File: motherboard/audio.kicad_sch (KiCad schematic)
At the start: 29 parts, among them CN1 PJ-332A-6A (3.5mm Jack), J3 RIGHT SPEAKERS, J4 LEFT SPEAKERS, Q12 2SK3018W, U23 TPA2028D1YZFT, U25 TPA2028D1YZFT

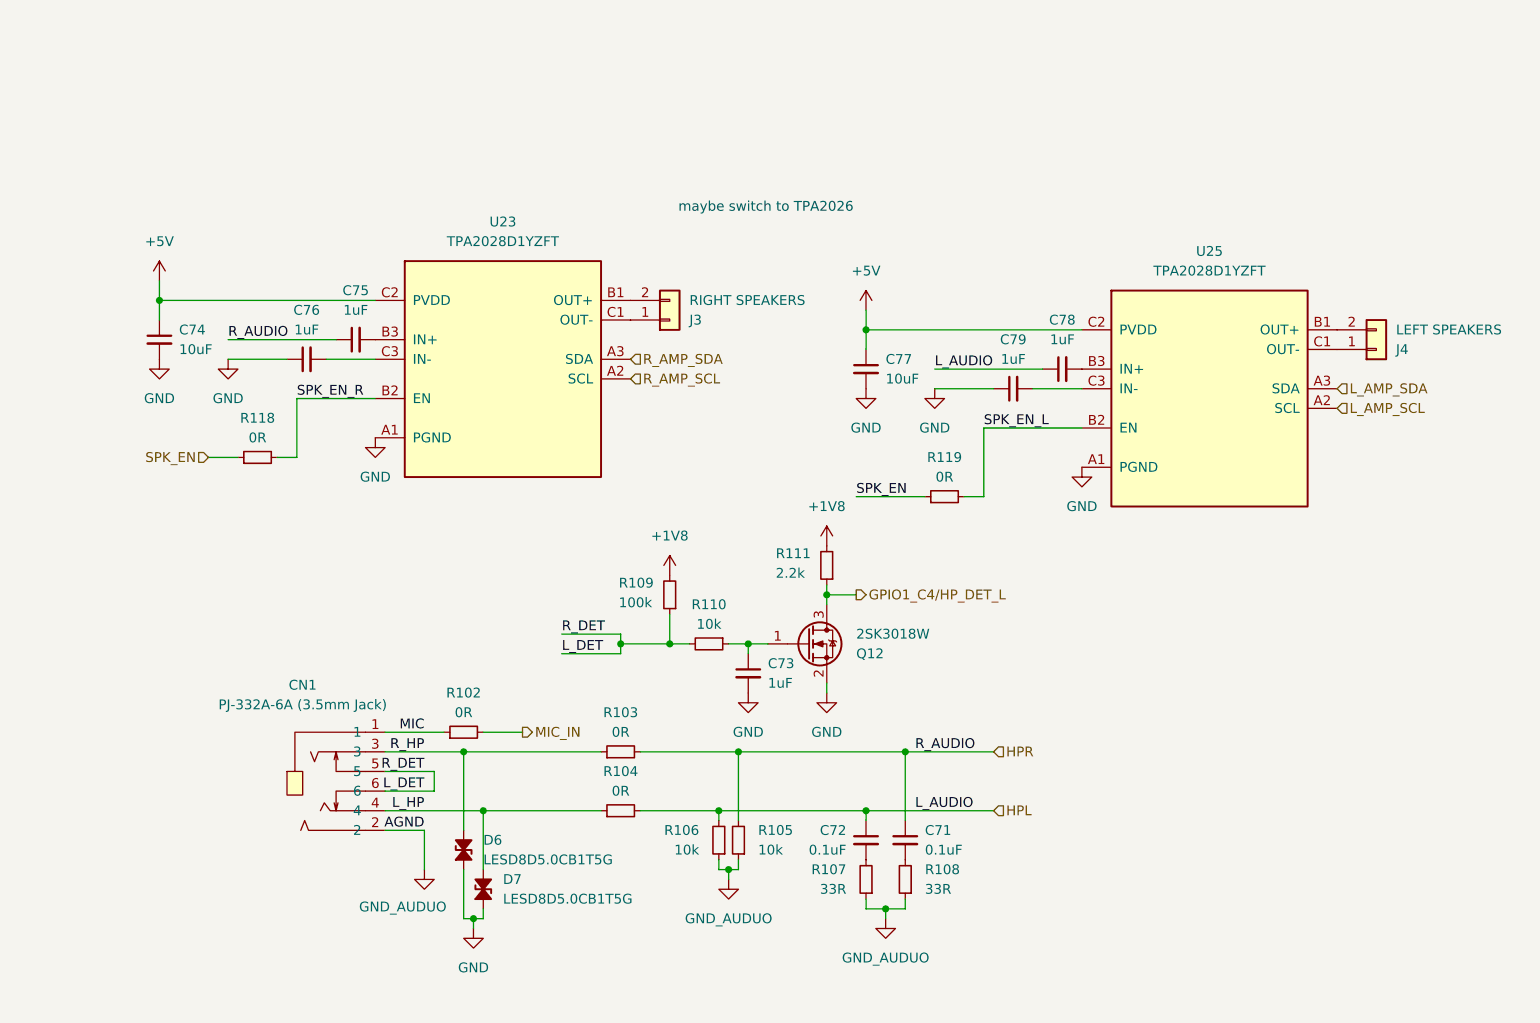
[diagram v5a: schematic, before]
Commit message: added two more display eval test boards
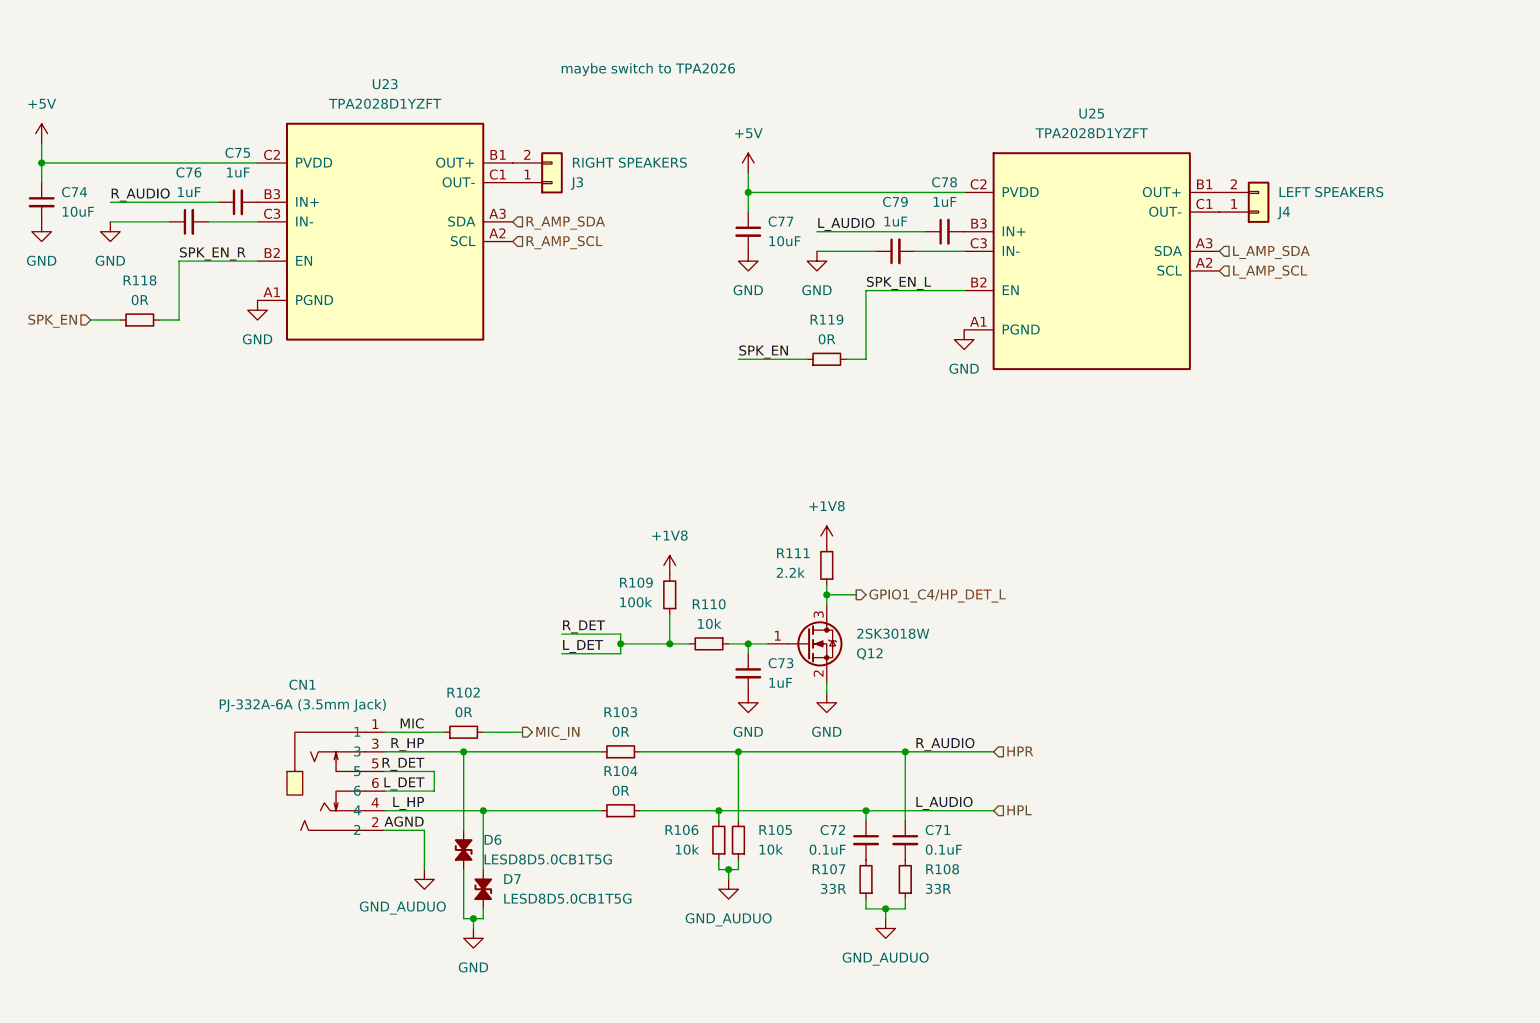
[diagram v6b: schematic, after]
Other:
- moved on the sheet: C74, C75, C76, C77, C78, C79, J3, J4, R118, R119, U23, U25

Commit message: starting motherboard v0.2
lessons from display eval v1
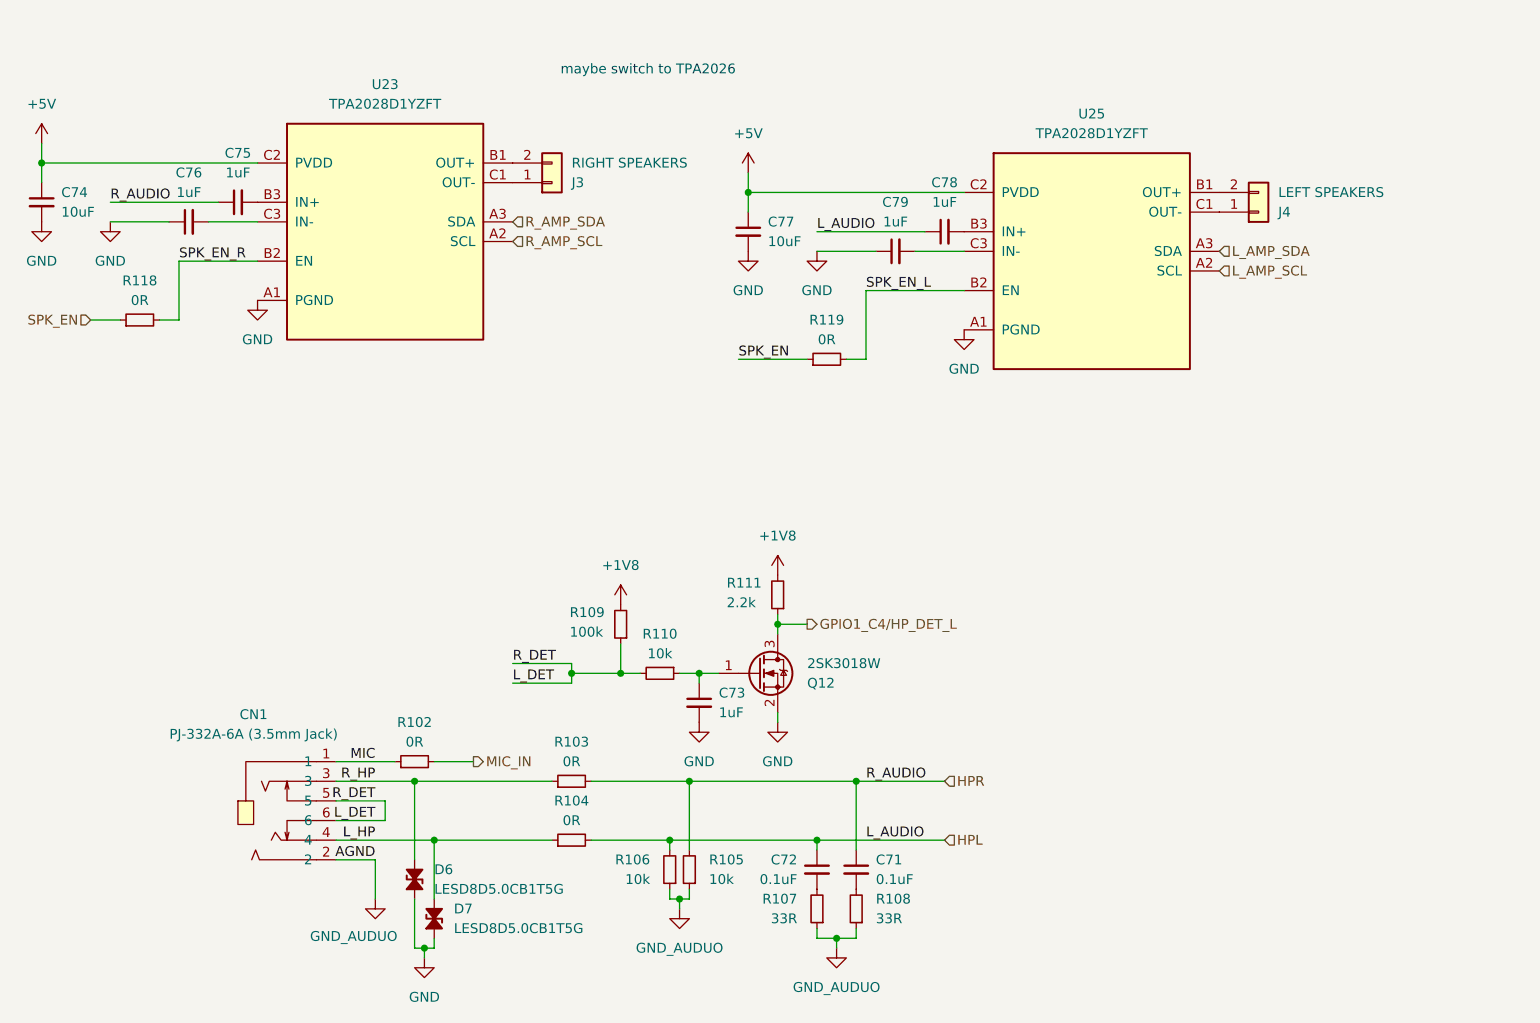
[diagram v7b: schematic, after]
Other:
- moved on the sheet: C71, C72, C73, CN1, D6, D7, Q12, R102, R103, R104, R105, R106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

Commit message: v0.2 layout
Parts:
- removed C74, C77: 10uF, Capacitor_SMD:C_0603_1608Metric, symbol Device:C_Small
- removed C75, C76, C78, C79: 1uF, Capacitor_SMD:C_0402_1005Metric, symbol Device:C_Small
- removed R118, R119: 0R, Resistor_SMD:R_0402_1005Metric, symbol Device:R_Small
- removed U23, U25: TPA2028D1YZFT, Audio_Amp:BGA9C50P3X3_162X162X63, symbol Audio_Amp:TPA2028D1YZFT
- added C33, C34, C35, C36: 1uF, Capacitor_SMD:C_0402_1005Metric, symbol Device:C_Small
- added C37: 10uF, Capacitor_SMD:C_0603_1608Metric, symbol Device:C_Small
- added C38: 0.1uF, Capacitor_SMD:C_0402_1005Metric, symbol Device:C_Small
- added FB1: GZ1608D601TF, Inductor_SMD:L_0603_1608Metric, symbol Device:FerriteBead_Small
- added U16: TPA2016D2RTJR, TPA2016:QFN50P400X400X80-21N, symbol TPS2016:TPA2016D2RTJR
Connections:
- net +5V: now also C37.1, C38.1, FB1.1, U16.11 (PVDDR_2), U16.12 (PVDDR), U16.4 (PVDDL_2), U16.5 (PVDDL)
- net GND: now also C37.2, C38.2, U16.21 (EP), U16.3 (AGND), U16.8 (PGND)
- net HPL: now also C33.1
- net HPR: now also C36.1
- net SPK_EN: now also U16.18 (SDZ)
- net at J3.1 (Pin_1): now also U16.9 (OUTR-)
- net at J3.2 (Pin_2): now also U16.10 (OUTR+)
- net at J4.2 (Pin_2): now also U16.6 (OUTL+)
- net at J4.1 (Pin_1): now also U16.7 (OUTL-)
- new net: C34.1, C35.1
- new net: C35.2, U16.14 (INR-)
- new net: C33.2, U16.1 (INL+)
- new net: FB1.2, U16.13 (AVDD)
- new net: C36.2, U16.15 (INR+)
- new net: C34.2, U16.2 (INL-)
- new net AMP_SCL: U16.19 (SDA)
- new net AMP_SDA: U16.17 (SCL)
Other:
- note removed: "maybe switch to TPA2026"
- moved on the sheet: C71, C72, C73, CN1, D6, D7, J3, J4, Q12, R102, R103, R104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
